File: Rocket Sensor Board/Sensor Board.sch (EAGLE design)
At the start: 115 parts, among them J1 501568-0207, J2 501568-0207, J3 SD-105027-101, J4 501568-0407, U1 MAG3110, U10 ADXL362, U11 TM4C1233H6PM, U12 TPS62082DSGR, U13 SN74AUP3G17, U15 ADT7301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

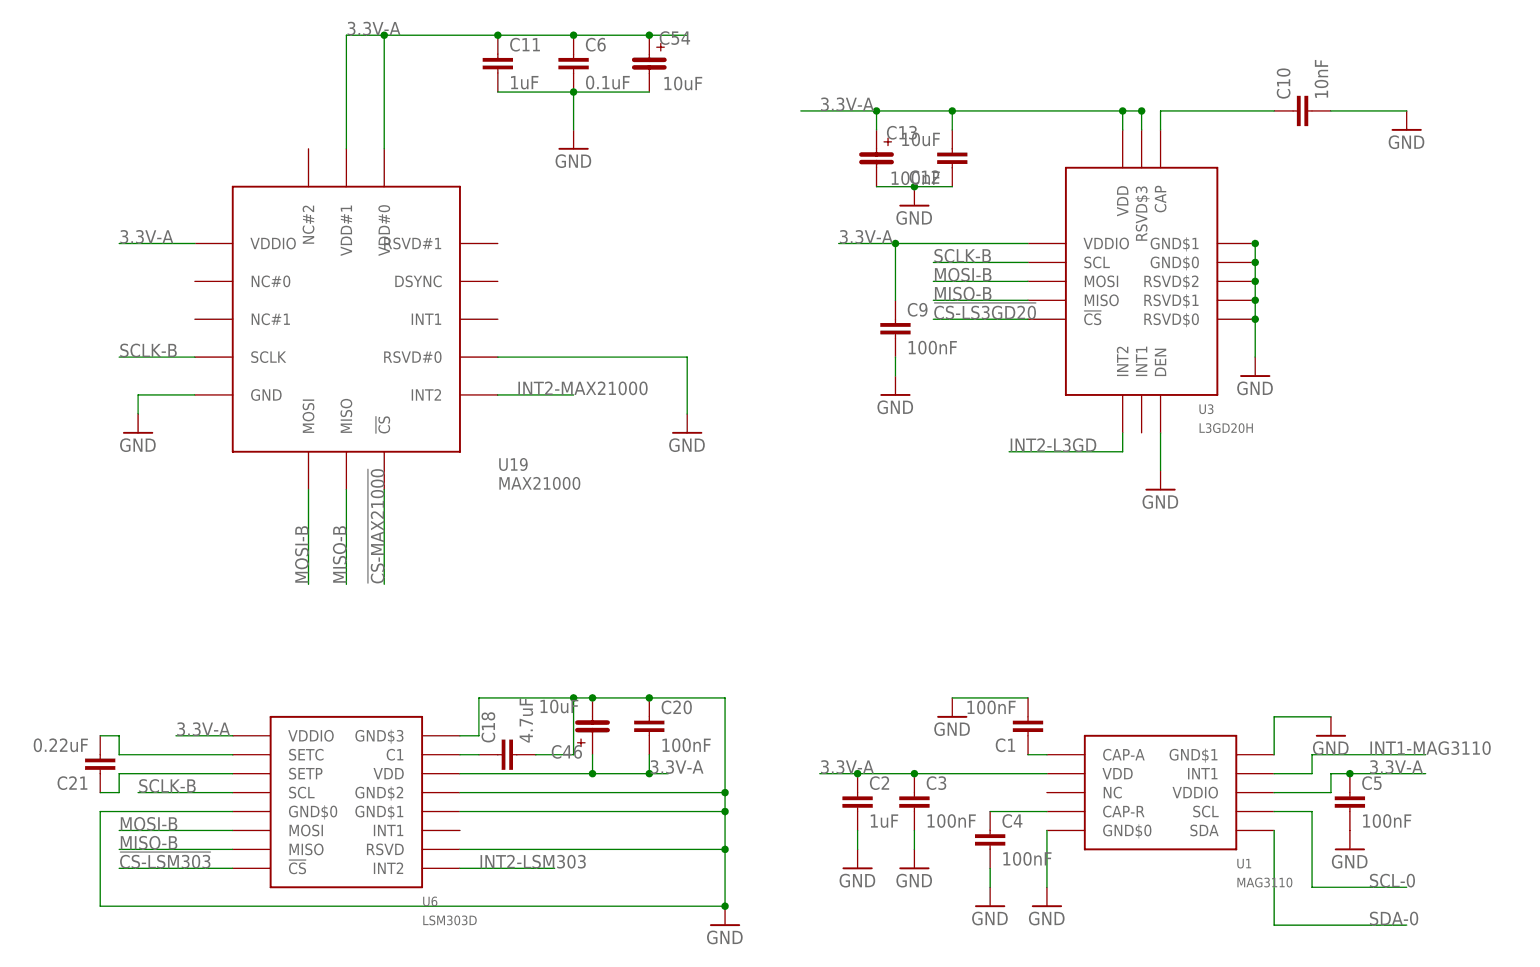
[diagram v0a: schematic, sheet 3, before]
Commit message: Rocket Sensor Board: Changed passives on LIS3DH, H3LIS331DLTR, L3GD20H, LSM303D, LSM9DS0, ADXL362 (But not the Tantalum), MAX2100 and Si7013 to use the new library parts with full documentaion and part numbers
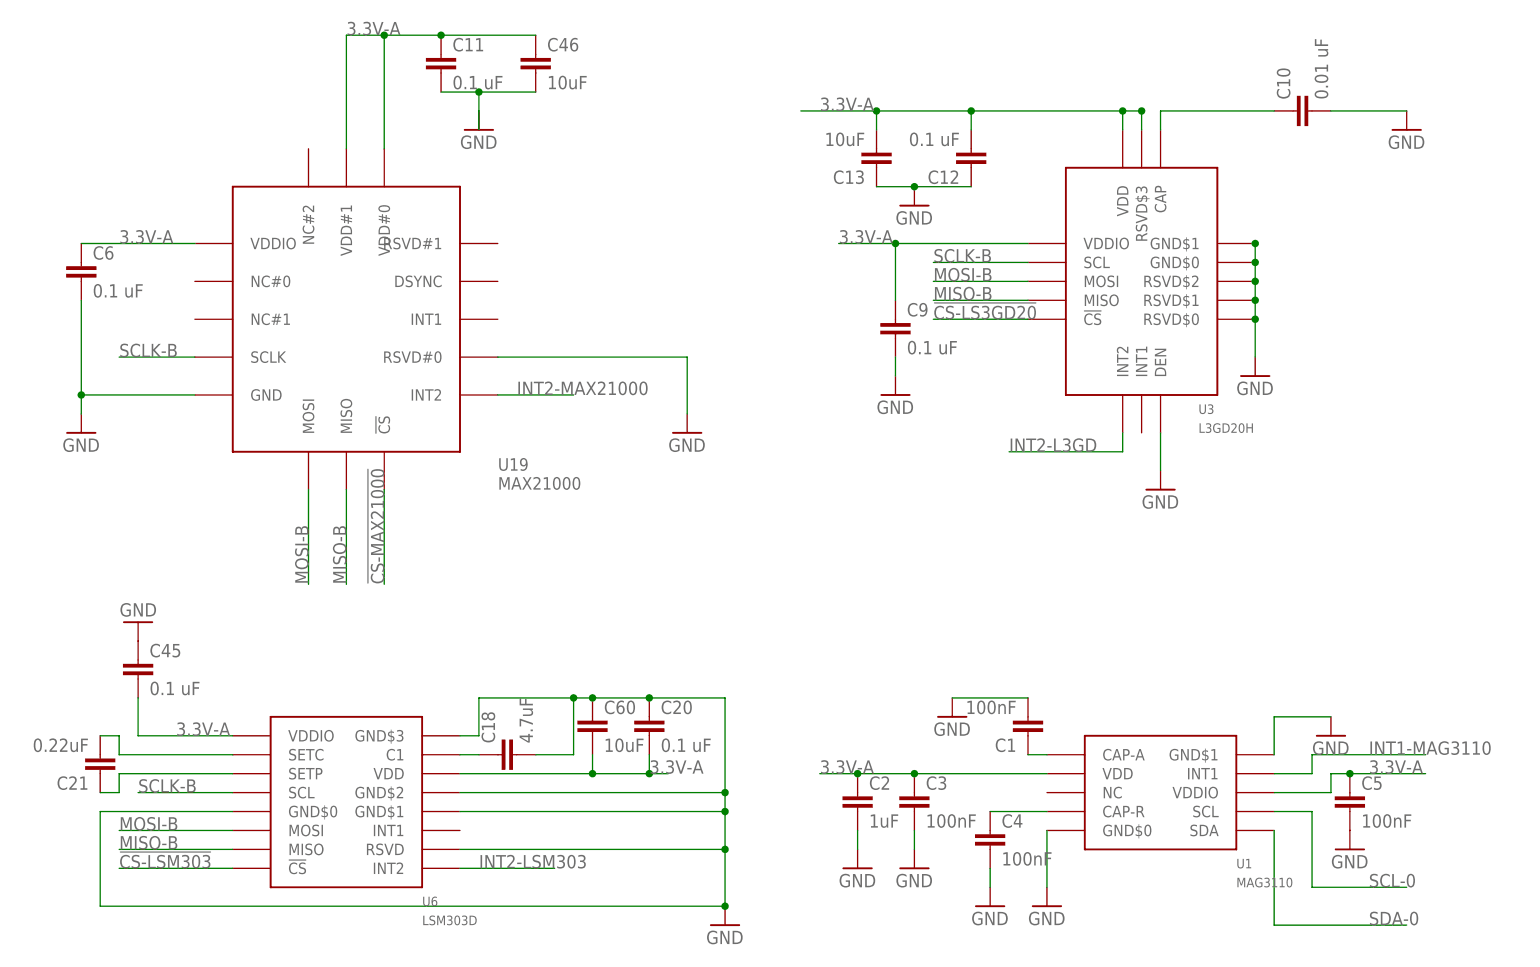
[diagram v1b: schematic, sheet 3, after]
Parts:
- removed C54: 10uF, Kas-Passives:EEFCD0J100ER
- added C57: 0.1 uF, Kas-Passives:CAPACITOR0.1U-X7R-10%-25V
- added C58, C59, C60: 10uF, Kas-Passives:CAPACITOR10U-X5R-10%-6.3V
- C10: value 10nF -> 0.01 uF; device Kas-Passives:CAPACITOR0402 -> Kas-Passives:CAPACITOR0.01U-X7R-10%-50V
- C11: value 1uF -> 0.1 uF; device Kas-Passives:CAPACITOR0402 -> Kas-Passives:CAPACITOR0.1U-X7R-10%-10V
- C12: value 10uF -> 0.1 uF; device Kas-Passives:CAPACITOR0402 -> Kas-Passives:CAPACITOR0.1U-X7R-10%-25V
- C13: value 100nF -> 10uF; device Kas-Passives:EEFCD0J100ER -> Kas-Passives:CAPACITOR10U-X5R-10%-6.3V
- C14, C20, C26, C8, C9: value 100nF -> 0.1 uF; device Kas-Passives:CAPACITOR0402 -> Kas-Passives:CAPACITOR0.1U-X7R-10%-25V
- C18: device Kas-Passives:CAPACITOR0402 -> Kas-Passives:CAPACITOR4.7U-X5R-10%-25V
- C21: device Kas-Passives:CAPACITOR0402 -> Kas-Passives:CAPACITOR0.22U-X7R-10%-50V
- C22: value 10uF -> 0.1 uF; device Kas-Passives:EEFCD0J100ER -> Kas-Passives:CAPACITOR0.1U-X7R-10%-10V
- C25, C46: device Kas-Passives:EEFCD0J100ER -> Kas-Passives:CAPACITOR10U-X5R-10%-10V
- C27: value 100nF -> 0.1 uF; device Kas-Passives:CAPACITOR0402 -> Kas-Passives:CAPACITOR0.1U-X7R-10%-16V
- C28, C29: value 0.1uF -> 0.1 uF; device Kas-Passives:CAPACITOR0402 -> Kas-Passives:CAPACITOR0.1U-X7R-10%-50V
- C45, C47: value 10uF -> 0.1 uF; device Kas-Passives:EEFCD0J100ER -> Kas-Passives:CAPACITOR0.1U-X7R-10%-25V
- C48: device Kas-Passives:CAPACITOR0402 -> Kas-Passives:CAPACITOR4.7U-Y5V--20+80-10V
- C51: value (none) -> 4.7 uF; device Kas-Passives:CAPACITOR0402 -> Kas-Passives:CAPACITOR4.7U-X5R-10%-6.3V
- C6: value 0.1uF -> 0.1 uF; device Kas-Passives:CAPACITOR0402 -> Kas-Passives:CAPACITOR0.1U-X7R-10%-10V
- C7: device Kas-Passives:EEFCD0J100ER -> Kas-Passives:CAPACITOR10U-X5R-10%-6.3V
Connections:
- net 3.3V-A: now also C13.2, C22.2, C25.1, C45.2, C46.1, C47.2, C57.1, C58.2, C59.2, C60.2, C7.1; no longer C13.@P$1, C22.@P$2, C25.@P$1, C45.@P$1, C46.@P$1, C47.@P$1, C54.@P$1, C7.@P$1
- net GND: now also C13.1, C22.1, C25.2, C45.1, C46.2, C47.1, C57.2, C58.1, C59.1, C60.1, C7.2; no longer C13.@P$2, C22.@P$1, C25.@P$2, C45.@P$2, C46.@P$2, C47.@P$2, C54.@P$2, C7.@P$2
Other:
- moved on the sheet: C11, C12, C6
